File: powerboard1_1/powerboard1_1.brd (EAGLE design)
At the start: 149.9 x 86.4 mm, 126 parts, among them Q1 IPP80P03P4L04AKSA1, Q2 2N4401TFR, Q3 2N4401TFR, Q4 2N4401TFR, U1 UWQ-12/20-T48NTB-C, U2 UWE-5/20-Q48NB-C, U3 UWE-3.3/30-Q48NB-C

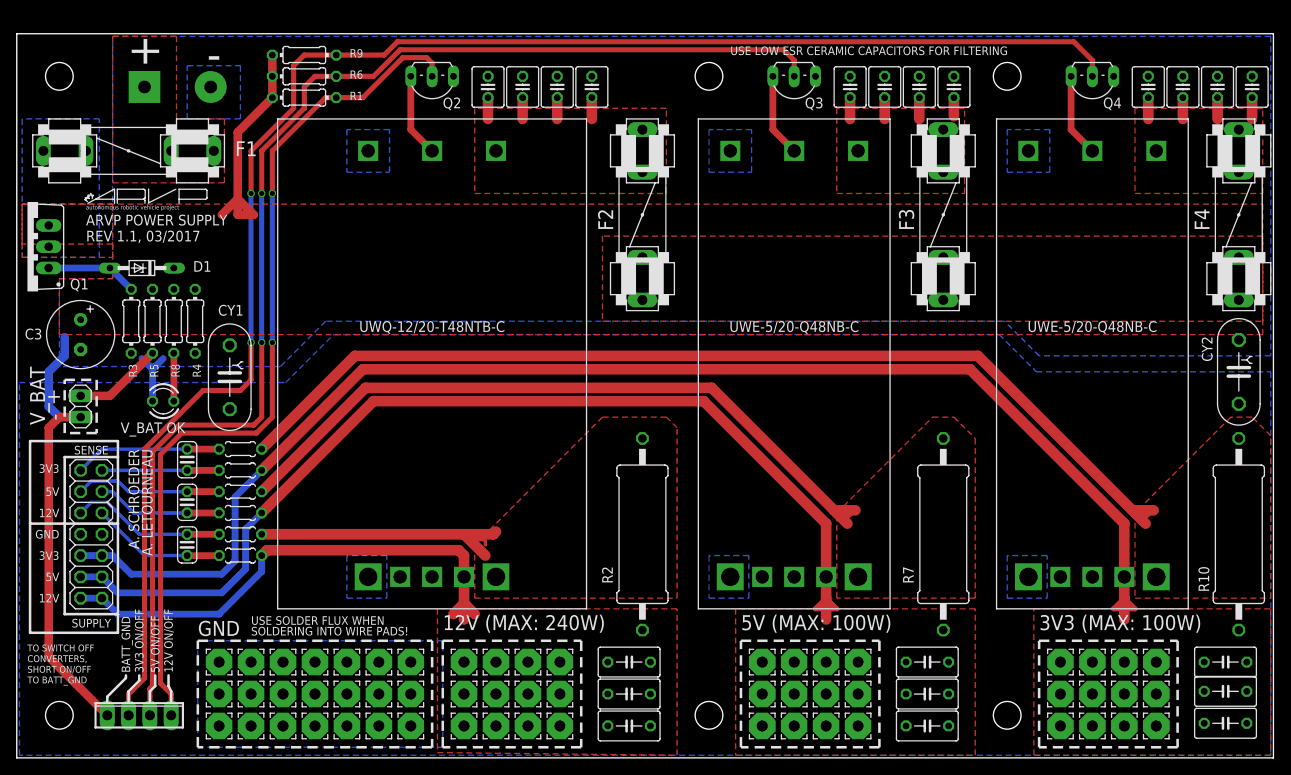
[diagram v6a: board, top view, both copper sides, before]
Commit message: Modifed some traces, texts, and graphics
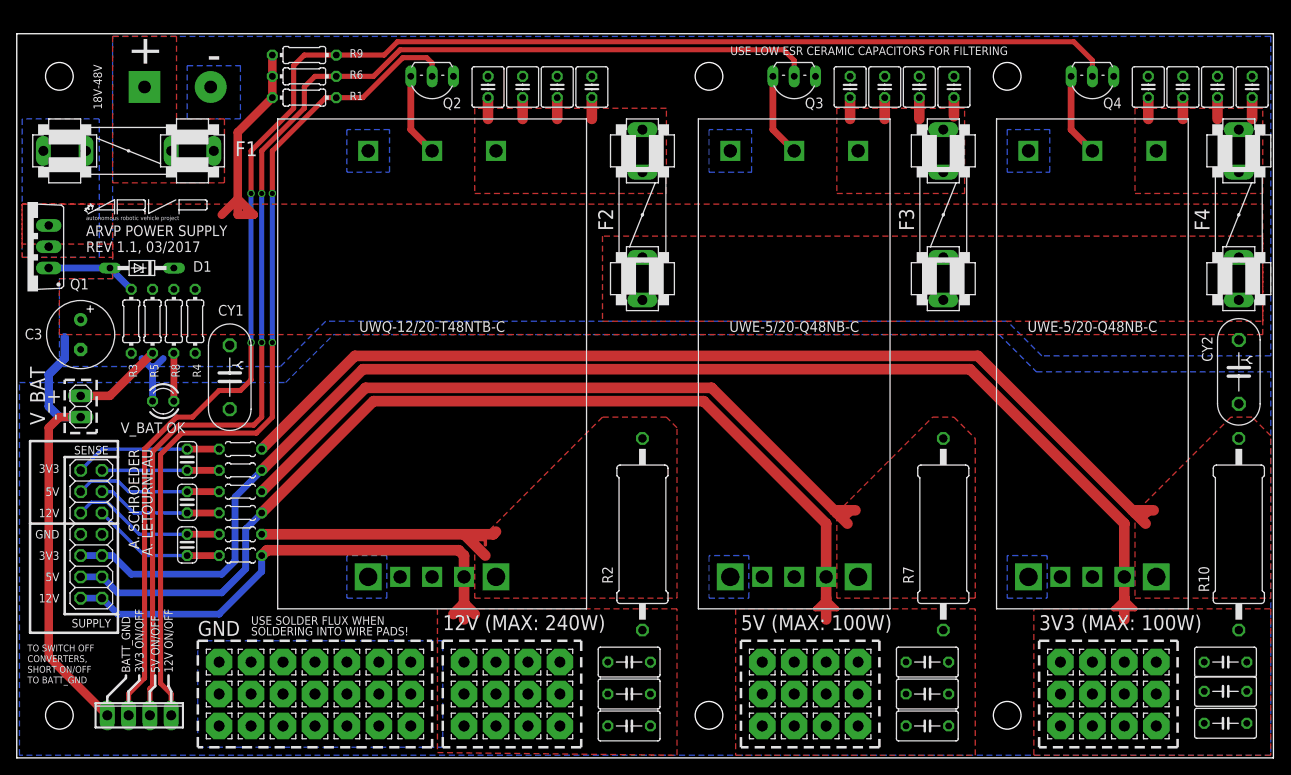
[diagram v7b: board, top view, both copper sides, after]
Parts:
- moved U$3 1.27 mm to (37.5, 55.2)
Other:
- board text added: "18V-48V"
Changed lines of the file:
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@@
 <?xml version="1.0" encoding="utf-8"?>
 <!DOCTYPE eagle SYSTEM "eagle.dtd">
-<eagle version="8.0.1">
+<eagle version="8.1.0">
 <drawing>
 <settings>
@@
 <wire x1="167.64" y1="5.08" x2="167.64" y2="-7.62" width="0.3048" layer="25" style="longdash"/>
 <wire x1="167.64" y1="-7.62" x2="151.13" y2="-7.62" width="0.3048" layer="25" style="longdash"/>
-<text x="37.465" y="54.61" size="1.27" layer="25">ARVP POWER SUPPLY</text>
+<text x="37.465" y="53.34" size="1.27" layer="25">ARVP POWER SUPPLY</text>
 <text x="44.1325" y="27.94" size="1.27" layer="25" rot="R270">A. LETOURNEAU</text>
 <text x="42.545" y="27.94" size="1.27" layer="25" rot="R270">A. SCHROEDER</text>
@@
 <text x="41.5925" y="29.845" size="1.27" layer="25">V_BAT OK</text>
 <text x="57.15" y="5.715" size="1.016" layer="25">SOLDERING INTO WIRE PADS!</text>
-<text x="37.465" y="52.705" size="1.27" layer="25">REV 1.1, 03/2017</text>
+<text x="37.465" y="51.435" size="1.27" layer="25">REV 1.1, 03/2017</text>
 <text x="30.48" y="0" size="0.8128" layer="25">TO BATT_GND</text>
 <text x="42.2275" y="1.27" size="1.016" layer="25" rot="R90" align="center-left">BATT_GND</text>
@@
 <text x="121.92" y="41.91" size="1.27" layer="25" align="bottom-center">UWE-5/20-Q48NB-C</text>
 <text x="157.48" y="41.91" size="1.27" layer="25" align="bottom-center">UWE-5/20-Q48NB-C</text>
+<text x="39.37" y="71.12" size="1.016" layer="25" rot="R90" align="bottom-center">18V-48V</text>
 </plain>
 <attributes>
@@
 <attribute name="VALUE" x="43.3451" y="41.5544" size="0.9906" layer="27" ratio="10" rot="R90"/>
 </element>
-<element name="U$3" library="ARVP" package="ARVP" value="" x="37.465" y="56.515"/>
+<element name="U$3" library="ARVP" package="ARVP" value="" x="37.465" y="55.245"/>
 <element name="JP7" library="pinhead" package="1X02" value="" x="36.83" y="33.02" smashed="yes" rot="R270">
 <attribute name="VALUE" x="33.655" y="35.56" size="1.27" layer="27" rot="R270"/>
@@
 <vertex x="178.7525" y="77.1525"/>
 <vertex x="178.7525" y="39.0525"/>
-<vertex x="151.13" y="39.0525"/>
-<vertex x="147.0025" y="43.18"/>
+<vertex x="151.4475" y="39.0525"/>
+<vertex x="147.32" y="43.18"/>
 <vertex x="66.04" y="43.18"/>
 <vertex x="60.6425" y="37.7825"/>
@@
 <wire x1="36.83" y1="31.75" x2="34.29" y2="31.75" width="1.016" layer="16"/>
 <wire x1="34.29" y1="31.75" x2="33.02" y2="33.02" width="1.016" layer="16"/>
-<wire x1="33.02" y1="33.02" x2="33.02" y2="37.1475" width="1.016" layer="16"/>
-<wire x1="33.02" y1="37.1475" x2="34.925" y2="39.0525" width="1.016" layer="16"/>
-<wire x1="34.925" y1="39.0525" x2="34.925" y2="41.275" width="1.016" layer="16"/>
+<wire x1="33.02" y1="33.02" x2="33.02" y2="36.83" width="1.016" layer="16"/>
+<wire x1="33.02" y1="36.83" x2="34.925" y2="38.735" width="1.016" layer="16"/>
+<wire x1="34.925" y1="38.735" x2="34.925" y2="41.275" width="1.016" layer="16"/>
 <contactref element="C3" pad="-"/>
 <contactref element="U1" pad="-VIN"/>
@@
 <wire x1="57.15" y1="40.64" x2="57.15" y2="36.195" width="0.6096" layer="1"/>
 <wire x1="57.15" y1="36.195" x2="55.88" y2="34.925" width="0.6096" layer="1"/>
-<wire x1="55.88" y1="34.925" x2="51.435" y2="34.925" width="0.6096" layer="1"/>
-<wire x1="51.435" y1="34.925" x2="44.45" y2="27.94" width="0.6096" layer="1"/>
+<wire x1="55.88" y1="34.925" x2="53.34" y2="34.925" width="0.6096" layer="1"/>
+<wire x1="53.34" y1="34.925" x2="50.165" y2="31.75" width="0.6096" layer="1"/>
+<wire x1="50.165" y1="31.75" x2="48.26" y2="31.75" width="0.6096" layer="1"/>
+<wire x1="48.26" y1="31.75" x2="44.45" y2="27.94" width="0.6096" layer="1"/>
 <wire x1="44.45" y1="27.94" x2="44.45" y2="0.635" width="0.6096" layer="1"/>
 <wire x1="44.45" y1="0.635" x2="42.545" y2="-1.27" width="0.6096" layer="1"/>

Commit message: Changed footprints of filtering capacitors and placed them closer to terminals; increased clearances between battery ground and output ground
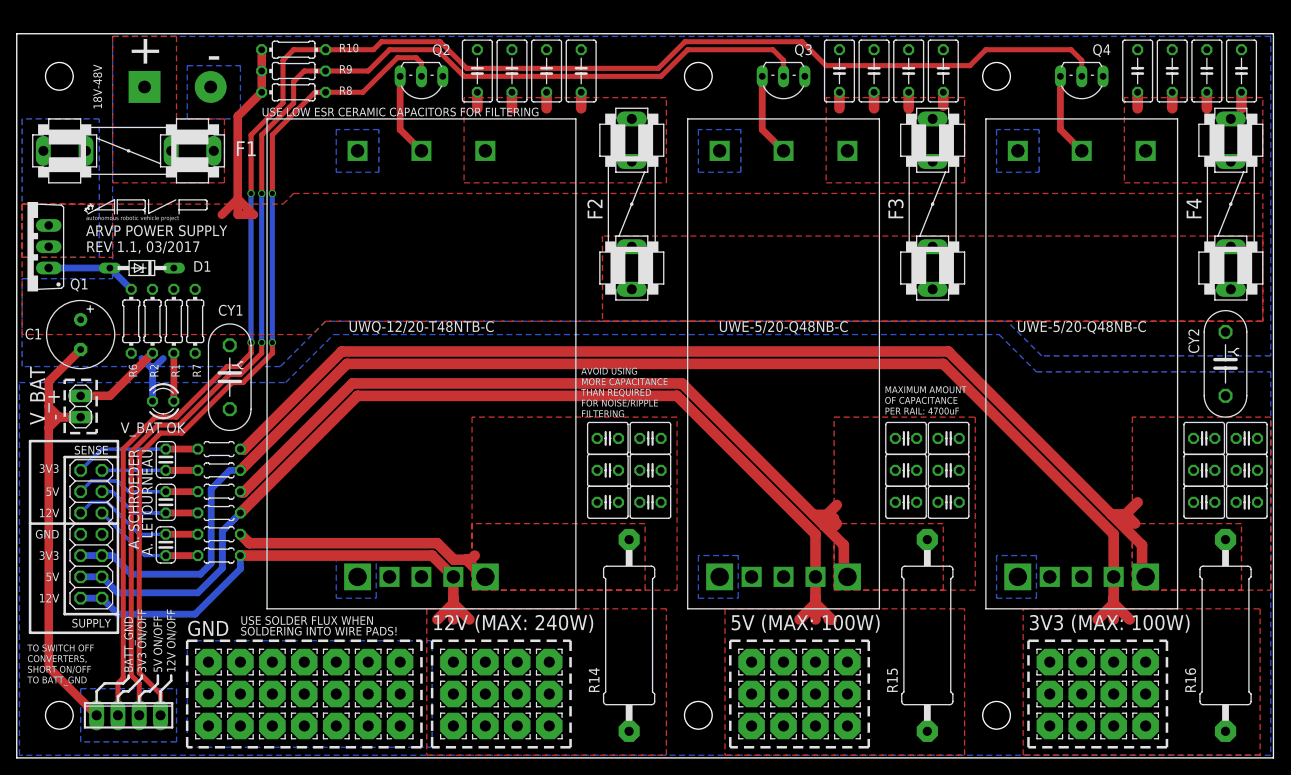
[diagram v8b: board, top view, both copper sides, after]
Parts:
- added C26, C27, C28, C29, C30, C31, C32, C33, C34: (no value), rcl:C025-040X050
- C1: value (none) -> 100u; device rcl:C025-040X050 -> rcl:E3,5-8
- C10, C11, C12, C16, C5, C9: device rcl:C025-040X050 -> rcl:C050-035X075
- C2, C4: value (none) -> 100n; device rcl:C025-040X050 -> rcl:C025-024X044
- C20, C21, C22: device rcl:C050-035X075 -> rcl:C025-040X050
- C23, C24, C25: value 100n -> (none); device rcl:C025-024X044 -> rcl:C025-040X050
- C3: value 100u -> 100n; device rcl:E3,5-8 -> rcl:C025-024X044
- R1: value 10k -> 36k
- R10: value 0.004 -> 10k; device rcl:0617/22 -> resistor:0204/7
- R14, R15, R16: value 10 -> 0.004; device rcl:0204/5 -> rcl:0617/22
- R2, R7: value 0.004 -> 4.7k; device rcl:0617/22 -> resistor:0204/7
- R3: value 2k -> 10; device resistor:0204/7 -> rcl:0204/5
- R4, R5: value 4.7k -> 10; device resistor:0204/7 -> rcl:0204/5
- R6: value 10k -> 2k
- R8: value 36k -> 10k
- moved R10 126.7 mm to (62.2, 75.6), turned to 0 degrees
- moved R16 119.6 mm to (173.4, 5.71), turned to 270 degrees
- moved PAD19 109.5 mm to (52.1, 2.54)
- moved PAD9 101.7 mm to (59.7, -1.27)
- moved PAD4 97.8 mm to (67.3, 2.54)
- moved PAD14 94.0 mm to (71.1, -5.08)
- moved R7 92.8 mm to (50.5, 43.2)
- moved C25 91.2 mm to (140.3, 25.4), turned to 0 degrees
- moved PAD46 87.7 mm to (163.8, 2.54)
- moved PAD50 87.7 mm to (156.2, -5.08)
- moved C15 84.9 mm to (171.1, 73.0), turned to 90 degrees
- moved R15 84.2 mm to (137.8, 5.71), turned to 270 degrees
- moved C17 83.8 mm to (104.8, 21.6), turned to 0 degrees
- moved C7 83.2 mm to (139.7, 73.0), turned to 90 degrees
- moved C8 82.0 mm to (127.3, 73.0), turned to 90 degrees
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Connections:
- net 12V+SENSE: now also C17.1, C18.1, C23.1, C24.1, C29.1, C30.1, R11.2, R14.1; no longer R12.2, R2.1
- net 12V-SENSE: now also PAD23.1, PAD24.1, PAD25.1, PAD26.1, PAD28.1, PAD29.1, PAD30.1, PAD31.1, PAD33.1, R14.2, R3.1; no longer C6.1, C7.1, C8.1, PAD12.1, PAD17.1, PAD2.1, PAD37.1, PAD42.1, PAD47.1, PAD52.1, PAD55.1, PAD7.1, R11.1, R2.2
- net 3V3+SENSE: now also C21.1, C22.1, C27.1, C28.1, C33.1, C34.1, R13.2, R16.1; no longer R10.1, R16.2
- net 3V3-SENSE: now also PAD46.1, PAD47.1, PAD48.1, PAD50.1, PAD51.1, PAD52.1, PAD53.1, PAD55.1, PAD56.1, R16.2, R5.1; no longer C20.1, C21.1, C22.1, PAD14.1, PAD19.1, PAD24.1, PAD29.1, PAD34.1, PAD39.1, PAD4.1, PAD44.1, PAD9.1, R10.2, R15.1
- net 5V+SENSE: now also C19.1, C20.1, C25.1, C26.1, C31.1, C32.1, R12.2, R15.1; no longer R14.2, R7.1
- net 5V-SENSE: now also PAD34.1, PAD35.1, PAD36.1, PAD37.1, PAD39.1, PAD40.1, PAD41.1, PAD42.1, PAD44.1, PAD45.1, R15.2, R4.1; no longer C13.1, C14.1, C15.1, PAD13.1, PAD18.1, PAD23.1, PAD28.1, PAD3.1, PAD33.1, PAD48.1, PAD53.1, PAD56.1, PAD8.1, R13.1, R7.2
- net GND: now also C17.2, C18.2, C19.2, C23.2, C24.2, C25.2, C26.2, C27.2, C28.2, C29.2, C30.2, C31.2, C32.2, C33.2, C34.2, PAD12.1, PAD13.1, PAD14.1, PAD17.1, PAD18.1, PAD19.1, PAD2.1, PAD3.1, PAD4.1, PAD7.1, PAD8.1, PAD9.1; no longer C13.2, C14.2, C15.2, C6.2, C7.2, C8.2, PAD25.1, PAD26.1, PAD30.1, PAD31.1, PAD35.1, PAD36.1, PAD40.1, PAD41.1, PAD45.1, PAD46.1, PAD50.1, PAD51.1
- net J3: now also C4.1, R3.2; no longer C25.1, R11.2
- net J4: now also C4.2, R11.1; no longer C25.2, R12.1
- net J5: now also C3.1, R4.2; no longer C24.1, R13.2
- net J6: now also C3.2, R12.1; no longer C24.2, R14.1
- net J7: now also C2.1, R5.2; no longer C23.1, R15.2
- net J8: now also C2.2, R13.1; no longer C23.2, R16.1
- net N$1: now also R1.1; no longer R8.1
- net N$12: now also C10.1, C15.1, C9.1; no longer C17.1, C18.1, C19.1
- net N$2: now also R2.2; no longer R5.2
- net N$4: now also R6.1; no longer R3.1
- net N$5: now also C11.1, C12.1, C6.1; no longer C1.1, C2.1, C4.1
- net N$7: now also C13.1, C14.1, C7.1, C8.1; no longer C10.1, C11.1, C12.1, C9.1
- net ON/OFF_1: now also R8.2; no longer R1.2
- net ON/OFF_2: now also R9.2; no longer R6.2
- net ON/OFF_3: now also R10.2; no longer R9.2
- net V+: now also C1.+, R1.2, R10.1, R2.1, R7.1, R8.1; no longer C3.+, R1.1, R4.1, R5.1, R6.1, R8.2
- net V-: now also C1.-, C13.2, C14.2, C15.2, C6.2, C7.2, C8.2, R6.2, R7.2; no longer C1.2, C17.2, C18.2, C19.2, C2.2, C3.-, C4.2, R3.2, R4.2
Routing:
- net 3V3+SENSE: track 122.1 -> 132.8 mm
- net 5V+SENSE: track 85.5 -> 95.7 mm
- net ON/OFF_3: track 187.5 -> 191.7 mm
- net V-: track 62.6 -> 65.2 mm
- net J8: track 17.6 -> 15.0 mm
- net J7: track 14.0 -> 11.4 mm
- net J6: track 17.6 -> 15.0 mm
- net J5: track 15.0 -> 12.5 mm
- net J4: track 18.6 -> 16.1 mm
- net J3: track 16.1 -> 13.5 mm
- net N$7: track 9.84 -> 7.30 mm
- net N$5: track 10.2 -> 7.62 mm
- net N$12: track 10.2 -> 7.62 mm
- net 12V+SENSE: track 34.2 -> 32.5 mm
- net ON/OFF_1: track 104.1 -> 102.5 mm
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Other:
- board text added: "AVOID USING"
- board text added: "FILTERING"
- board text added: "FOR NOISE/RIPPLE"
- board text added: "MAXIMUM AMOUNT"
- board text added: "MORE CAPACITANCE"
- board text added: "OF CAPACITANCE"
- board text added: "PER RAIL: 4700uF"
- board text added: "THAN REQUIRED"
